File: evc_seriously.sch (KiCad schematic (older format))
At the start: 58 parts, among them J1 Screw_Terminal_01x10, J2 Conn_ARM_JTAG_SWD_10, J3 J_IN, J4 J_OUT, SW1 SW_Push, U1 TCA9517, U2 MPM3510A, U3 MPM3510A, U4 STM32F303K8Tx, U5 MIC2981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

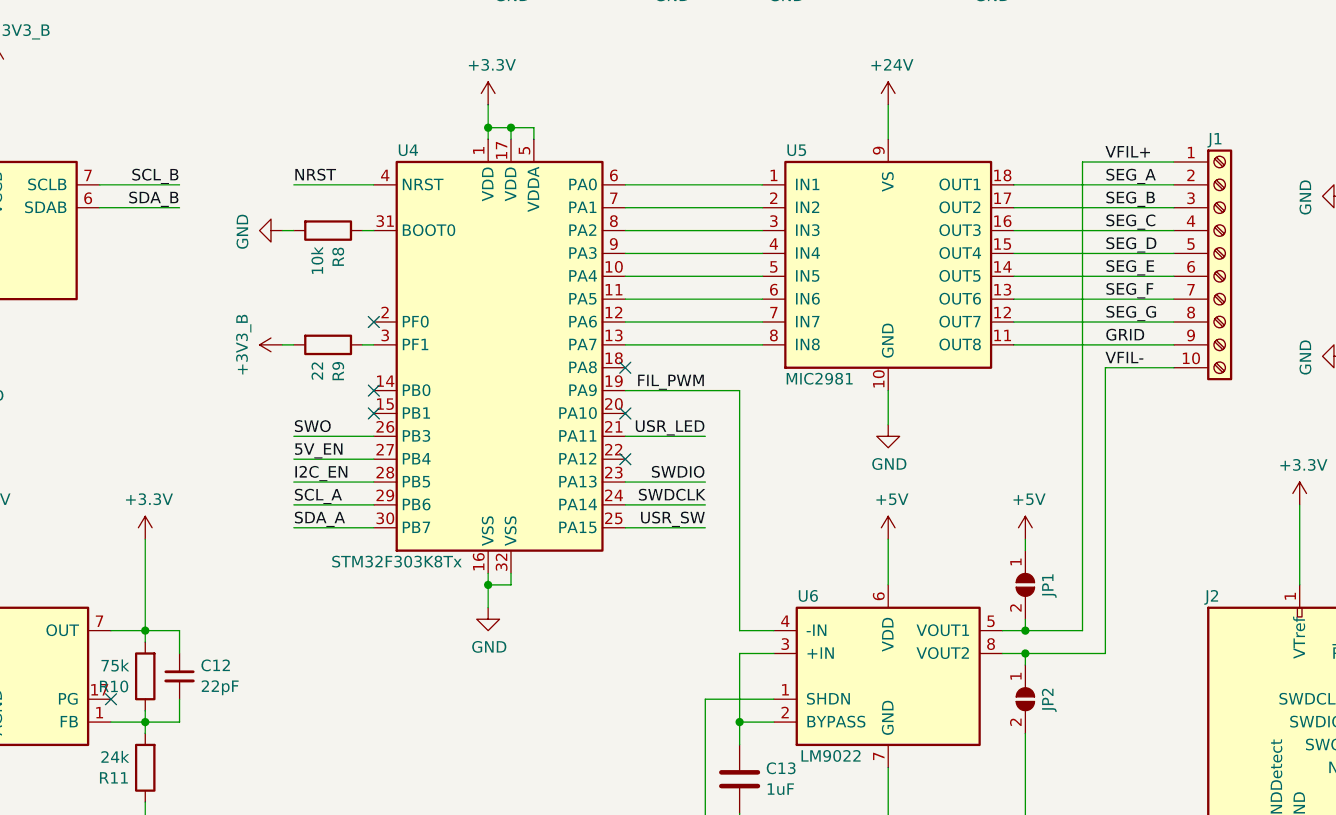
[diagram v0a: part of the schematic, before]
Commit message: More routing
- Swapped position of 3V3 and 5V buck converters
- Finish routing power nets
- Start routing data/enable lines
- Swap a bunch of microcontroller pins to reduce hopping
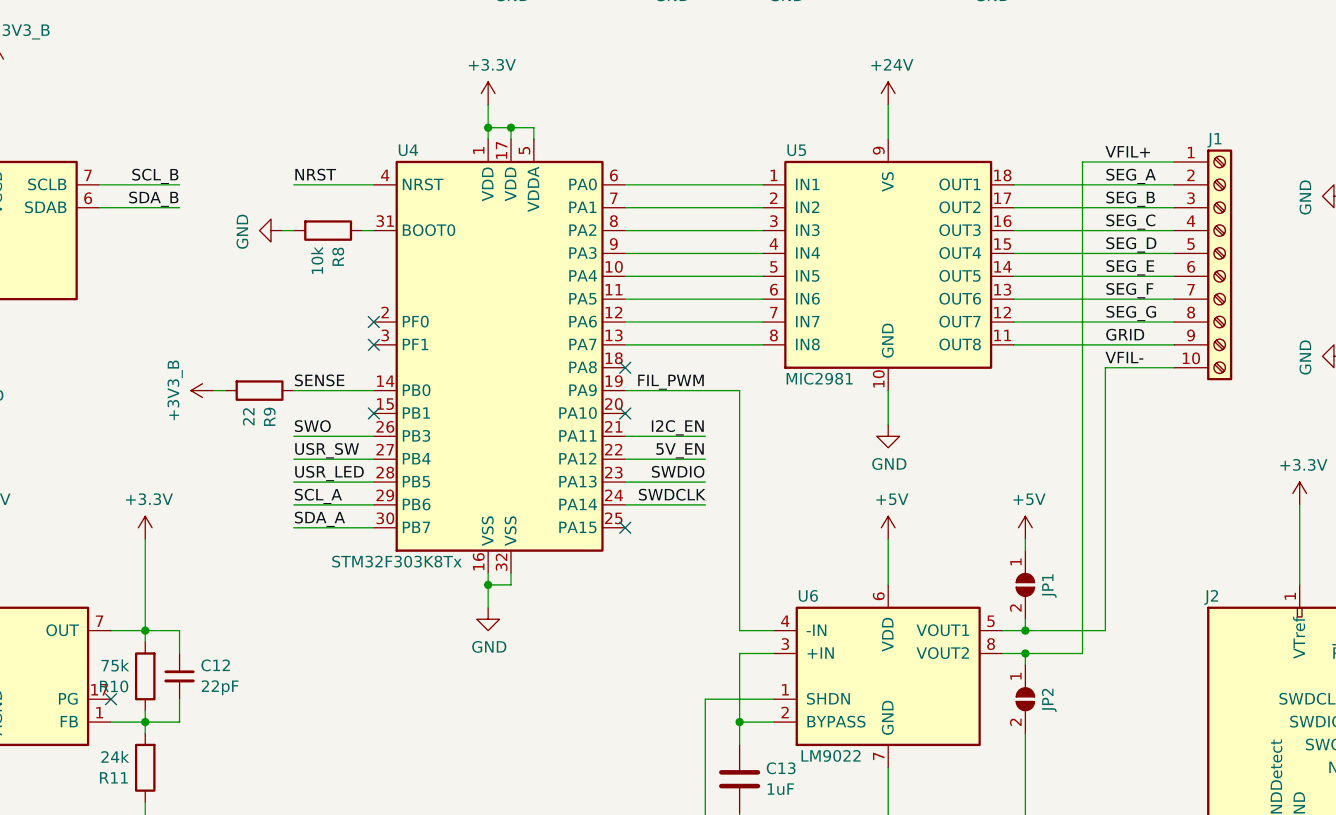
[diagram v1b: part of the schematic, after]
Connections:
- net 5V_EN: now also U4.22 (PA12); no longer U4.27 (PB4)
- net I2C_EN: now also U4.21 (PA11); no longer U4.28 (PB5)
- net USR_LED: now also U4.28 (PB5); no longer U4.21 (PA11)
- net USR_SW: now also U4.27 (PB4); no longer U4.25 (PA15)
- net VFIL+: now also JP2.1 (A), U6.8 (VOUT2); no longer JP1.2 (B), U6.5 (VOUT1)
- net VFIL-: now also JP1.2 (B), U6.5 (VOUT1); no longer JP2.1 (A), U6.8 (VOUT2)
- net SENSE: now reaches U4.14 (PB0)
- net SENSE: now also R9.1
- net at U4.3 (PF1): no longer R9.1
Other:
- moved on the sheet: R9
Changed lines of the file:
@@
 	7400 3950 7400 3800
-Wire Wire Line
-	8650 3700 8350 3700
 Wire Wire Line
 	8250 2800 8650 2800
@@
 	6750 5250 6900 5250
 Wire Wire Line
-	8000 4950 8350 4950
-Wire Wire Line
-	8350 4950 8350 3700
-Wire Wire Line
-	8250 4850 8250 2800
+	8000 4950 8250 4950
 Connection ~ 8000 4950
 Wire Wire Line
 	8000 4950 8000 5000
 Wire Wire Line
-	8000 4850 8250 4850
+	8000 4850 8350 4850
 Connection ~ 8000 4850
 Wire Wire Line
@@
 	1    0    0    -1
 $EndComp
-NoConn ~ 6250 4100
+NoConn ~ 6250 4400
 NoConn ~ 6250 3700
-NoConn ~ 5150 3800
 NoConn ~ 5150 3500
-Text Label 6600 4000 2    50   ~ 0
+Text Label 4800 4200 0    50   ~ 0
 USR_LED
-Wire Wire Line
-	6250 4000 6600 4000
 Text Label 4800 4000 0    50   ~ 0
 SWO
 Wire Wire Line
-	5150 4000 4800 4000
-Wire Wire Line
-	4750 3600 4800 3600
-$Comp
-L evc_seriously:+3V3_B #PWR021
-U 1 1 5FFE7843
-P 4750 3600
-F 0 "#PWR021" H 4750 3450 50  0001 C CNN
-F 1 "+3V3_B" H 4750 3775 50  0000 C CNN
-F 2 "" H 4750 3600 50  0001 C CNN
-F 3 "" H 4750 3600 50  0001 C CNN
-	1    4750 3600
-	0    -1   -1   0
-$EndComp
-Wire Wire Line
-	5150 3600 5100 3600
-Wire Wire Line
-	4800 4100 5150 4100
-Wire Wire Line
-	4800 4200 5150 4200
-$Comp
-L Device:R R9
-U 1 1 5FD8C22C
-P 4950 3600
-F 0 "R9" H 5020 3646 50  0000 L CNN
-F 1 "22" H 5020 3555 50  0000 L CNN
-F 2 "Resistor_SMD:R_0603_1608Metric" V 4880 3600 50  0001 C CNN
-F 3 "~" H 4950 3600 50  0001 C CNN
-	1    4950 3600
-	0    1    1    0
-$EndComp
-Wire Wire Line
-	4800 2900 5150 2900
-Wire Wire Line
 	4750 3100 4800 3100
 Wire Wire Line
@@
 Wire Wire Line
 	6850 2900 6250 2900
-Wire Wire Line
-	5150 4400 4800 4400
-Wire Wire Line
-	5150 4300 4800 4300
 Wire Wire Line
 	6250 4200 6600 4200
@@
 Text Label 4800 4300 0    50   ~ 0
 SCL_A
-Text Label 4800 4200 0    50   ~ 0
+Text Label 6600 4000 2    50   ~ 0
 I2C_EN
-Text Label 4800 4100 0    50   ~ 0
+Text Label 6600 4100 2    50   ~ 0
 5V_EN
 Text Label 6600 3800 2    50   ~ 0
@@
 Connection ~ 1250 1300
 NoConn ~ 5150 3900
-Text Label 6600 4400 2    50   ~ 0
+Text Label 4800 4100 0    50   ~ 0
 USR_SW
 Wire Wire Line
 	5650 2550 5650 2650
+NoConn ~ 6250 3900
+Wire Wire Line
+	6600 4000 6250 4000
+Wire Wire Line
+	6600 4100 6250 4100
+Wire Wire Line
+	5150 4400 4800 4400
+Wire Wire Line
+	5150 4300 4800 4300
+Wire Wire Line
+	5150 4100 4800 4100
+Wire Wire Line
+	5150 4000 4800 4000
+Wire Wire Line
+	4800 2900 5150 2900
 $Comp
 L MCU_ST_STM32F3:STM32F303K8Tx U4
@@
 	1    0    0    -1
 $EndComp
-NoConn ~ 6250 3900
-Wire Wire Line
-	6600 4400 6250 4400
+Wire Wire Line
+	4800 4200 5150 4200
+$Comp
+L Device:R R9
+U 1 1 5FD8C22C
+P 4650 3800
+F 0 "R9" H 4720 3846 50  0000 L CNN
+F 1 "22" H 4720 3755 50  0000 L CNN
+F 2 "Resistor_SMD:R_0603_1608Metric" V 4580 3800 50  0001 C CNN
+F 3 "~" H 4650 3800 50  0001 C CNN
+	1    4650 3800
+	0    1    1    0
+$EndComp
+$Comp
+L evc_seriously:+3V3_B #PWR021
+U 1 1 5FFE7843
+P 4450 3800
+F 0 "#PWR021" H 4450 3650 50  0001 C CNN
+F 1 "+3V3_B" H 4450 3975 50  0000 C CNN
+F 2 "" H 4450 3800 50  0001 C CNN
+F 3 "" H 4450 3800 50  0001 C CNN
+	1    4450 3800
+	0    -1   -1   0
+$EndComp
+Wire Wire Line
+	4450 3800 4500 3800
+NoConn ~ 5150 3600
+Wire Wire Line
+	4800 3800 5150 3800
+Text Label 4800 3800 0    50   ~ 0
+SENSE
+Wire Wire Line
+	8350 3700 8350 4850
+Wire Wire Line
+	8350 3700 8650 3700
+Wire Wire Line
+	8250 4950 8250 2800
 $EndSCHEMATC

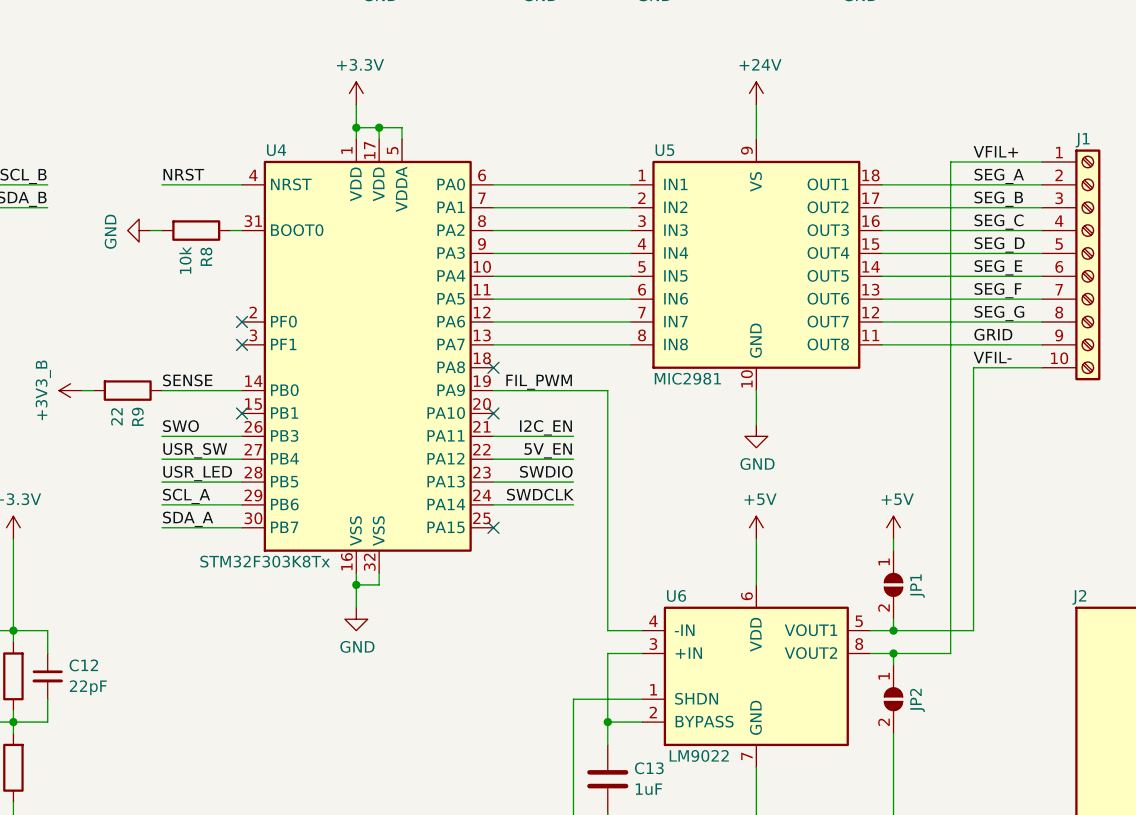
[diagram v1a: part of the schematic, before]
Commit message: Finish board routing, tidy silkscreen
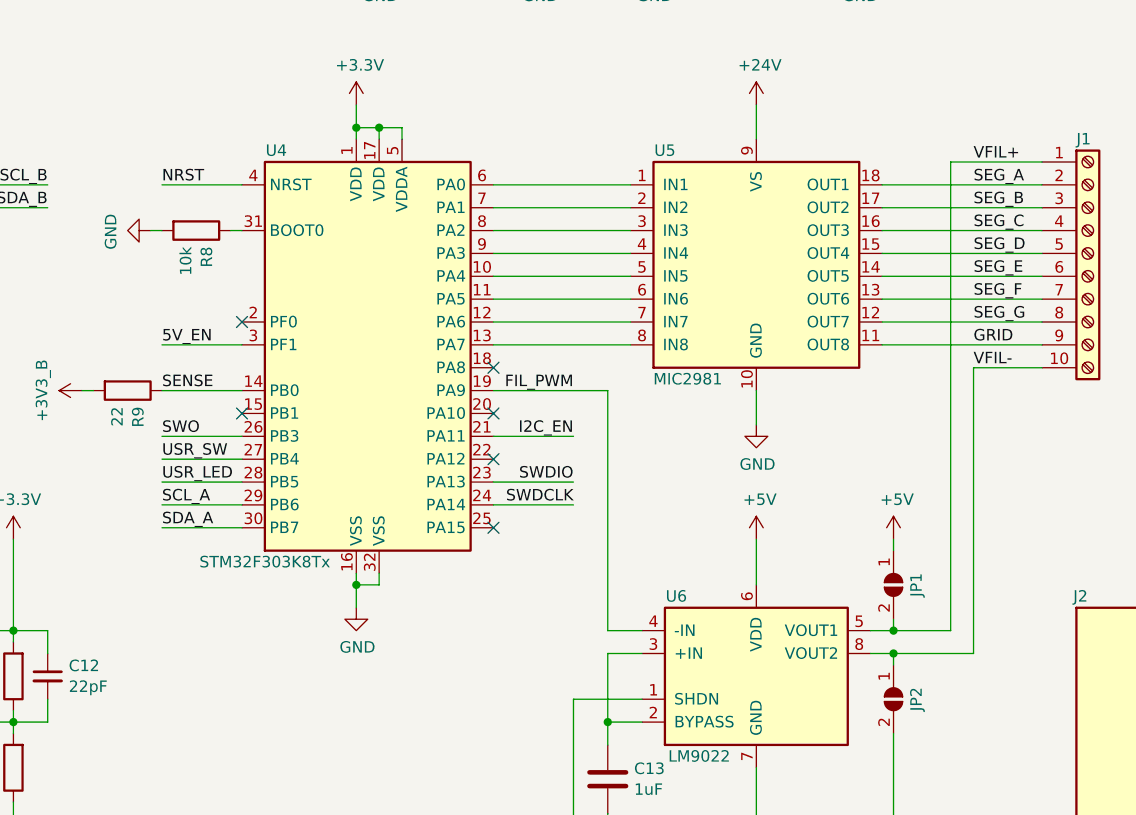
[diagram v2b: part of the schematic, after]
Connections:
- net 5V_EN: now also U4.3 (PF1); no longer U4.22 (PA12)
- net VFIL+: now also JP1.2 (B), U6.5 (VOUT1); no longer JP2.1 (A), U6.8 (VOUT2)
- net VFIL-: now also JP2.1 (A), U6.8 (VOUT2); no longer JP1.2 (B), U6.5 (VOUT1)
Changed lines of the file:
@@
 	6750 5250 6900 5250
 Wire Wire Line
-	8000 4950 8250 4950
+	8000 4950 8350 4950
 Connection ~ 8000 4950
 Wire Wire Line
 	8000 4950 8000 5000
 Wire Wire Line
-	8000 4850 8350 4850
+	8000 4850 8250 4850
 Connection ~ 8000 4850
 Wire Wire Line
@@
 Text Label 6600 4000 2    50   ~ 0
 I2C_EN
-Text Label 6600 4100 2    50   ~ 0
+Text Label 4800 3600 0    50   ~ 0
 5V_EN
 Text Label 6600 3800 2    50   ~ 0
@@
 	6600 4000 6250 4000
 Wire Wire Line
-	6600 4100 6250 4100
-Wire Wire Line
 	5150 4400 4800 4400
 Wire Wire Line
@@
 Wire Wire Line
 	4450 3800 4500 3800
-NoConn ~ 5150 3600
+NoConn ~ 6250 4100
 Wire Wire Line
 	4800 3800 5150 3800
@@
 SENSE
 Wire Wire Line
-	8350 3700 8350 4850
+	5150 3600 4800 3600
+Wire Wire Line
+	8350 4950 8350 3700
 Wire Wire Line
 	8350 3700 8650 3700
 Wire Wire Line
-	8250 4950 8250 2800
+	8250 4850 8250 2800
 $EndSCHEMATC
